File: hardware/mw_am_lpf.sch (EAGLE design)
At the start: 15 parts, among them J1 VGA_DB25

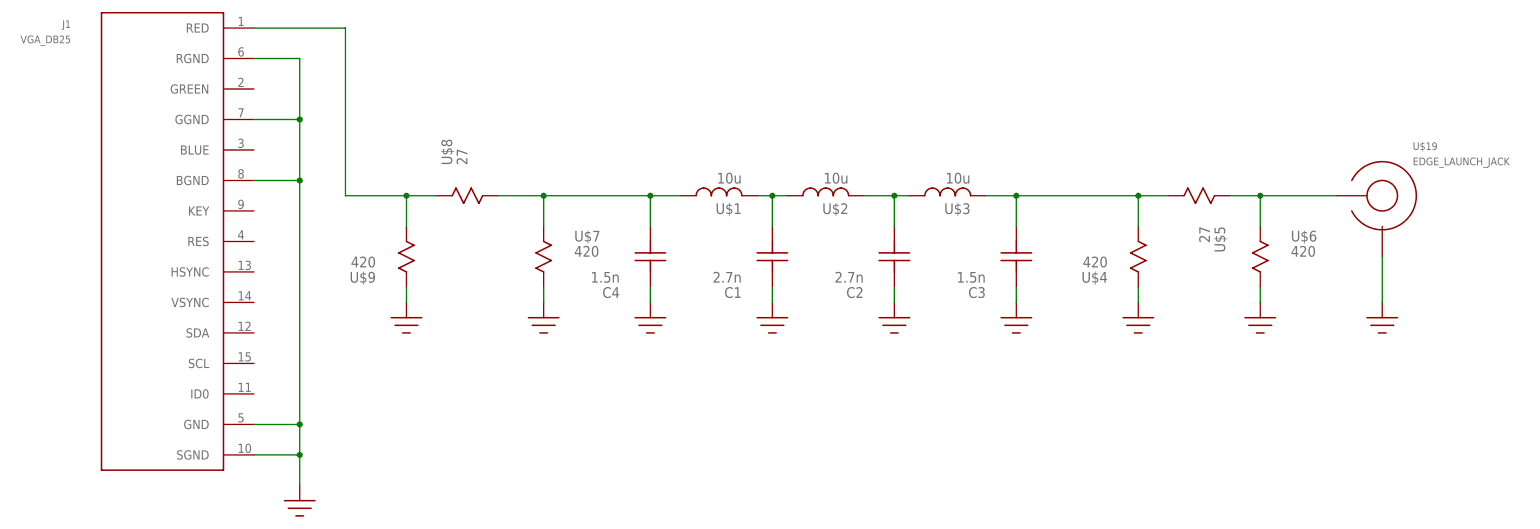
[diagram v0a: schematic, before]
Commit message: added PTH for VGA connector tabs; LPF has SMA jack
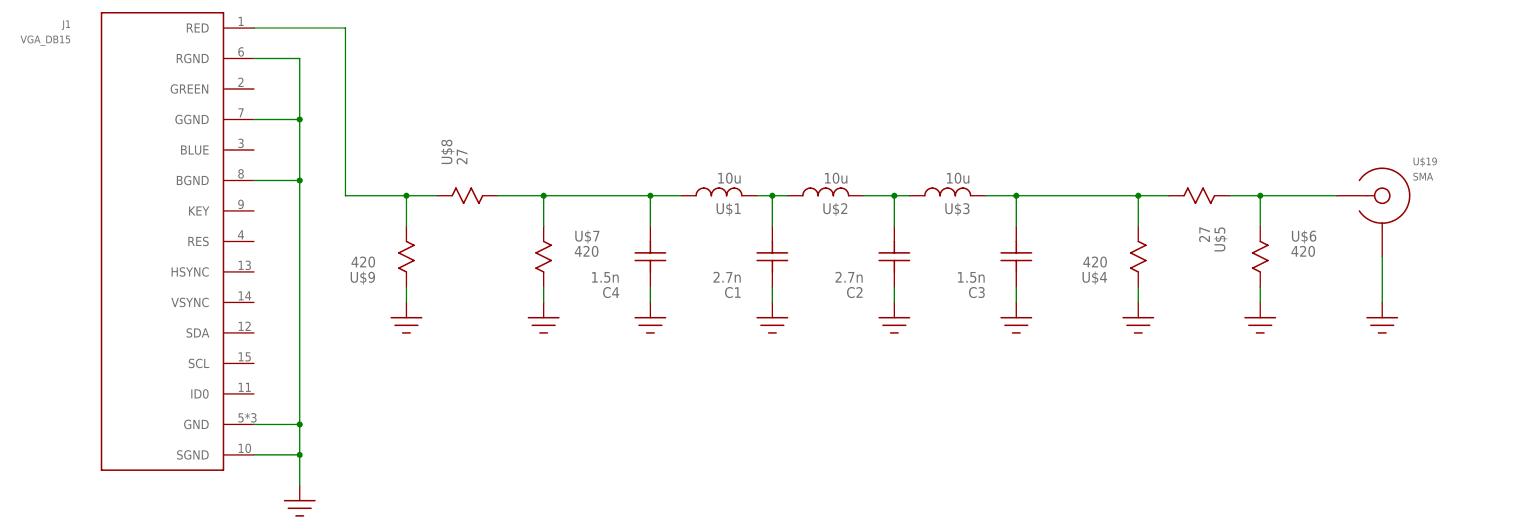
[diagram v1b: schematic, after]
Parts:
- J1: value VGA_DB25 -> VGA_DB15; device mw-voice-marker:VGA_DB25 -> mw-voice-marker:VGA_DB15
- U$19: value EDGE_LAUNCH_JACK -> SMA
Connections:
- net GND: now also U$19.SHIELD; no longer U$19.GND
- net N$5: now also U$19.CENTER; no longer U$19.SIG
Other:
- moved on the sheet: J1
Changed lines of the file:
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@@
 <grid distance="0.1" unitdist="inch" unit="inch" style="lines" multiple="1" display="no" altdistance="0.01" altunitdist="inch" altunit="inch"/>
 <layers>
-<layer number="1" name="Top" color="4" fill="1" visible="yes" active="no"/>
-<layer number="2" name="Route2" color="1" fill="3" visible="yes" active="no"/>
-<layer number="15" name="Route15" color="4" fill="6" visible="yes" active="no"/>
-<layer number="16" name="Bottom" color="1" fill="1" visible="yes" active="no"/>
-<layer number="17" name="Pads" color="2" fill="1" visible="yes" active="no"/>
-<layer number="18" name="Vias" color="2" fill="1" visible="yes" active="no"/>
-<layer number="19" name="Unrouted" color="6" fill="1" visible="yes" active="no"/>
-<layer number="20" name="Dimension" color="24" fill="1" visible="yes" active="no"/>
-<layer number="21" name="tPlace" color="7" fill="1" visible="yes" active="no"/>
-<layer number="22" name="bPlace" color="7" fill="1" visible="yes" active="no"/>
-<layer number="23" name="tOrigins" color="15" fill="1" visible="yes" active="no"/>
-<layer number="24" name="bOrigins" color="15" fill="1" visible="yes" active="no"/>
-<layer number="25" name="tNames" color="7" fill="1" visible="yes" active="no"/>
-<layer number="26" name="bNames" color="7" fill="1" visible="yes" active="no"/>
-<layer number="27" name="tValues" color="7" fill="1" visible="yes" active="no"/>
-<layer number="28" name="bValues" color="7" fill="1" visible="yes" active="no"/>
+<layer number="1" name="Top" color="4" fill="1" visible="no" active="no"/>
+<layer number="2" name="Route2" color="1" fill="3" visible="no" active="no"/>
+<layer number="15" name="Route15" color="4" fill="6" visible="no" active="no"/>
+<layer number="16" name="Bottom" color="1" fill="1" visible="no" active="no"/>
+<layer number="17" name="Pads" color="2" fill="1" visible="no" active="no"/>
+<layer number="18" name="Vias" color="2" fill="1" visible="no" active="no"/>
+<layer number="19" name="Unrouted" color="6" fill="1" visible="no" active="no"/>
+<layer number="20" name="Dimension" color="24" fill="1" visible="no" active="no"/>
+<layer number="21" name="tPlace" color="7" fill="1" visible="no" active="no"/>
+<layer number="22" name="bPlace" color="7" fill="1" visible="no" active="no"/>
+<layer number="23" name="tOrigins" color="15" fill="1" visible="no" active="no"/>
+<layer number="24" name="bOrigins" color="15" fill="1" visible="no" active="no"/>
+<layer number="25" name="tNames" color="7" fill="1" visible="no" active="no"/>
+<layer number="26" name="bNames" color="7" fill="1" visible="no" active="no"/>
+<layer number="27" name="tValues" color="7" fill="1" visible="no" active="no"/>
+<layer number="28" name="bValues" color="7" fill="1" visible="no" active="no"/>
 <layer number="29" name="tStop" color="7" fill="3" visible="no" active="no"/>
 <layer number="30" name="bStop" color="7" fill="6" visible="no" active="no"/>
@@
 <layer number="35" name="tGlue" color="7" fill="4" visible="no" active="no"/>
 <layer number="36" name="bGlue" color="7" fill="5" visible="no" active="no"/>
-<layer number="37" name="tTest" color="7" fill="1" visible="yes" active="no"/>
-<layer number="38" name="bTest" color="7" fill="1" visible="yes" active="no"/>
+<layer number="37" name="tTest" color="7" fill="1" visible="no" active="no"/>
+<layer number="38" name="bTest" color="7" fill="1" visible="no" active="no"/>
 <layer number="39" name="tKeepout" color="4" fill="11" visible="no" active="no"/>
 <layer number="40" name="bKeepout" color="1" fill="11" visible="no" active="no"/>
@@
 <layer number="44" name="Drills" color="7" fill="1" visible="no" active="no"/>
 <layer number="45" name="Holes" color="7" fill="1" visible="no" active="no"/>
-<layer number="46" name="Milling" color="3" fill="1" visible="yes" active="no"/>
-<layer number="47" name="Measures" color="7" fill="1" visible="yes" active="no"/>
-<layer number="48" name="Document" color="7" fill="1" visible="yes" active="no"/>
-<layer number="49" name="Reference" color="7" fill="1" visible="yes" active="no"/>
-<layer number="51" name="tDocu" color="7" fill="1" visible="yes" active="no"/>
-<layer number="52" name="bDocu" color="7" fill="1" visible="yes" active="no"/>
+<layer number="46" name="Milling" color="3" fill="1" visible="no" active="no"/>
+<layer number="47" name="Measures" color="7" fill="1" visible="no" active="no"/>
+<layer number="48" name="Document" color="7" fill="1" visible="no" active="no"/>
+<layer number="49" name="Reference" color="7" fill="1" visible="no" active="no"/>
+<layer number="51" name="tDocu" color="7" fill="1" visible="no" active="no"/>
+<layer number="52" name="bDocu" color="7" fill="1" visible="no" active="no"/>
 <layer number="88" name="SimResults" color="9" fill="1" visible="yes" active="yes"/>
 <layer number="89" name="SimProbes" color="9" fill="1" visible="yes" active="yes"/>
@@
 <part name="U$16" library="mw-voice-marker" deviceset="GND" device=""/>
 <part name="U$17" library="mw-voice-marker" deviceset="GND" device=""/>
-<part name="J1" library="mw-voice-marker" deviceset="VGA_DB25" device=""/>
+<part name="J1" library="mw-voice-marker" deviceset="VGA_DB15" device=""/>
 <part name="U$18" library="mw-voice-marker" deviceset="GND" device=""/>
-<part name="U$19" library="mw-voice-marker" deviceset="EDGE_LAUNCH_JACK" device=""/>
 <part name="U$20" library="mw-voice-marker" deviceset="GND" device=""/>
+<part name="U$19" library="mw-voice-marker" deviceset="EDGE_LAUNCH_JACK" device="" value="SMA"/>
 </parts>
 <sheets>
@@
 <instance part="J1" gate="G$1" x="-53.34" y="48.26" rot="MR0"/>
 <instance part="U$18" gate="G$1" x="-27.94" y="7.62"/>
+<instance part="U$20" gate="G$1" x="152.4" y="38.1"/>
 <instance part="U$19" gate="G$1" x="152.4" y="55.88"/>
-<instance part="U$20" gate="G$1" x="152.4" y="38.1"/>
 </instances>
 <busses>
@@
 <segment>
 <pinref part="U$20" gate="G$1" pin="GND"/>
-<pinref part="U$19" gate="G$1" pin="GND"/>
 <wire x1="152.4" y1="38.1" x2="152.4" y2="45.72" width="0.1524" layer="91"/>
+<pinref part="U$19" gate="G$1" pin="SHIELD"/>
 </segment>
 </net>
@@
 <pinref part="U$6" gate="G$1" pin="P$3"/>
 <wire x1="132.08" y1="55.88" x2="132.08" y2="50.8" width="0.1524" layer="91"/>
-<pinref part="U$19" gate="G$1" pin="SIG"/>
 <wire x1="144.78" y1="55.88" x2="132.08" y2="55.88" width="0.1524" layer="91"/>
 <junction x="132.08" y="55.88"/>
-</segment>
-</net>
+<pinref part="U$19" gate="G$1" pin="CENTER"/>
+</segment>
+</net>
